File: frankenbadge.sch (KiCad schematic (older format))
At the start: 42 parts, among them IC101 PIC32MX270, P101 CONN_01X05, P102 USB_A, Q101 Q_NPN_BEC, Q102 Q_NPN_BEC, SW101 SW_PUSH, U101 4MHz resonator, U102 MCP1623/24, U103 MCP1700T, U104 TSOP362, U105 TouchSensor, U106 TouchSensor, Y101 32.768kHz

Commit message: cleaned up some caps and jumpers
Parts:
- removed C111: 0.1u, symbol C_Small
- added R101, R102, R113: 0R0, symbol R_Small
- added R107: 1K0, symbol R_Small
- C110: value 1u -> 0.1u
- renumbered R101 to R103, R102 to R104, R103 to R105, R104 to R106, R105 to R108, R106 to R109, R107 to R110, R108 to R111, R109 to R112, R110 to R114, R111 to R115, R112 to R116, R113 to R117
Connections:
- wire segments 164 -> 171
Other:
- moved on the sheet: C110

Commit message: updated boost converter parts and added screen interface
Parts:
- BT101: symbol Battery -> Battery-RESCUE-frankenbadge
- C103: value Cin -> 4.7u
- C105: value Cout -> 10u
- D101: symbol LED -> LED-RESCUE-frankenbadge
- D102: symbol LED_RGB -> LED_RGB-RESCUE-frankenbadge
- L101: value L_Small -> 4.7 uH; Fieldname (none) -> Value
- P102: symbol USB_A -> USB_A-RESCUE-frankenbadge
- R103: value Rt -> 3011
- R104: value Rb -> 6041
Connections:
- net labels added: /CS, /RES, AO, LEDK, SCA, SCK
- wire segments 171 -> 178
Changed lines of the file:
@@
 $Descr A4 11693 8268
 encoding utf-8
-Sheet 1 1
+Sheet 1 2
 Title ""
 Date ""
@@
 $EndComp
 $Comp
-L Battery BT101
+L Battery-RESCUE-frankenbadge BT101
 U 1 1 58485CE3
 P 720 940
@@
 P 960 930
 F 0 "C103" H 970 1000 50  0000 L CNN
-F 1 "Cin" H 970 850 50  0000 L CNN
+F 1 "4.7u" H 970 850 50  0000 L CNN
 F 2 "" H 960 930 50  0000 C CNN
 F 3 "" H 960 930 50  0000 C CNN
@@
 P 1170 690
 F 0 "L101" V 1120 650 50  0000 L CNN
-F 1 "L_Small" V 1240 540 50  0000 L CNN
+F 1 "4.7 uH" V 1240 540 50  0000 L CNN
 F 2 "" H 1170 690 50  0000 C CNN
 F 3 "" H 1170 690 50  0000 C CNN
+F 4 "Value" H 1170 690 60  0001 C CNN "Fieldname"
 	1    1170 690
 	0    -1   -1   0
@@
 P 2230 910
 F 0 "R103" H 2260 930 50  0000 L CNN
-F 1 "Rt" H 2260 870 50  0000 L CNN
+F 1 "3011" H 2260 870 50  0000 L CNN
 F 2 "" H 2230 910 50  0000 C CNN
 F 3 "" H 2230 910 50  0000 C CNN
@@
 P 2230 1170
 F 0 "R104" H 2260 1190 50  0000 L CNN
-F 1 "Rb" H 2260 1130 50  0000 L CNN
+F 1 "6041" H 2260 1130 50  0000 L CNN
 F 2 "" H 2230 1170 50  0000 C CNN
 F 3 "" H 2230 1170 50  0000 C CNN
@@
 P 2460 1010
 F 0 "C105" H 2470 1080 50  0000 L CNN
-F 1 "Cout" H 2230 1010 50  0000 L CNN
+F 1 "10u" H 2230 1010 50  0000 L CNN
 F 2 "" H 2460 1010 50  0000 C CNN
 F 3 "" H 2460 1010 50  0000 C CNN
@@
 $EndComp
 $Comp
-L USB_A P102
+L USB_A-RESCUE-frankenbadge P102
 U 1 1 5848AEBB
 P 8520 2570
@@
 	1960 3860 1750 3860
 Wire Wire Line
-	1750 3860 1750 3820
-Wire Wire Line
-	1750 3820 870  3820
+	1750 3820 1750 3860
+Wire Wire Line
+	870  3820 1750 3820
 Wire Wire Line
 	1960 3980 1750 3980
 Wire Wire Line
-	1750 3980 1750 4020
-Wire Wire Line
-	1750 4020 870  4020
+	1750 4020 1750 3980
+Wire Wire Line
+	870  4020 1750 4020
 Connection ~ 1510 4020
 Connection ~ 1510 3820
@@
 Connection ~ 2640 6180
 $Comp
-L LED_RGB D102
+L LED_RGB-RESCUE-frankenbadge D102
 U 1 1 5848EC5B
 P 5630 3310
@@
 	4460 6300 4460 6300
 $Comp
-L LED D101
+L LED-RESCUE-frankenbadge D101
 U 1 1 58491021
 P 4770 5900
@@
 $EndComp
 Wire Wire Line
-	5690 2570 4720 2570
-Wire Wire Line
-	4720 2570 4720 3770
-Wire Wire Line
-	4720 3770 3960 3770
+	5690 2570 4800 2570
+Wire Wire Line
+	4800 2570 4800 3770
+Wire Wire Line
+	4800 3770 3960 3770
 $Comp
 L +3.3V #PWR122
@@
 $EndComp
 Wire Wire Line
-	3960 3870 4360 3870
-Wire Wire Line
-	4360 3870 4360 1860
-Wire Wire Line
-	4360 1860 6770 1860
-Wire Wire Line
-	4500 2040 6770 2040
-Wire Wire Line
-	4500 2040 4500 3970
-Wire Wire Line
-	4500 3970 3960 3970
+	3960 3870 4695 3870
+Wire Wire Line
+	4695 3870 4695 1860
+Wire Wire Line
+	4695 1860 6770 1860
+Wire Wire Line
+	4765 2045 6770 2040
+Wire Wire Line
+	4765 2045 4765 3975
+Wire Wire Line
+	4765 3975 3960 3970
 $Comp
 L GND #PWR128
@@
 	7370 1370 7370 2240
 Wire Wire Line
-	3960 3570 4070 3570
-Wire Wire Line
-	4070 3570 4070 1280
-Wire Wire Line
-	4070 1280 6770 1280
-Wire Wire Line
-	6770 1460 4180 1460
-Wire Wire Line
-	4180 1460 4180 3670
-Wire Wire Line
-	4180 3670 3960 3670
+	3960 3570 4465 3570
+Wire Wire Line
+	4465 3570 4465 1280
+Wire Wire Line
+	4465 1280 6770 1280
+Wire Wire Line
+	6770 1460 4610 1460
+Wire Wire Line
+	4610 1460 4610 3670
+Wire Wire Line
+	4610 3670 3960 3670
 Connection ~ 7370 1950
 $Comp
@@
 Wire Wire Line
 	5150 2380 5040 2380
+$Sheet
+S 8675 4100 1505 1235
+U 591A14A3
+F0 "screen" 60
+F1 "screen.sch" 60
+F2 "/CS" I L 8675 5045 60
+F3 "SCK" I L 8675 4325 60
+F4 "SDA" I L 8675 4520 60
+F5 "AO" I L 8675 4690 60
+F6 "/RESET" I L 8675 4865 60
+F7 "PWR" I L 8675 4175 60
+F8 "LEDK" I L 8675 5230 60
+$EndSheet
+$Comp
+L +3.3V #PWR?
+U 1 1 591A3ACB
+P 8365 4175
+F 0 "#PWR?" H 8365 4025 50  0001 C CNN
+F 1 "+3.3V" H 8365 4315 50  0000 C CNN
+F 2 "" H 8365 4175 50  0000 C CNN
+F 3 "" H 8365 4175 50  0000 C CNN
+F 4 "Value" H 8365 4175 60  0001 C CNN "Fieldname"
+	1    8365 4175
+	1    0    0    -1
+$EndComp
+Wire Wire Line
+	8675 4175 8365 4175
+Wire Wire Line
+	8675 4325 8120 4325
+Wire Wire Line
+	8675 4520 8120 4520
+Wire Wire Line
+	8675 4690 8120 4690
+Wire Wire Line
+	8675 4865 8120 4865
+Wire Wire Line
+	8675 5045 8120 5045
+Wire Wire Line
+	8675 5230 8120 5230
+Text Label 8120 4325 0    60   ~ 0
+SCK
+Text Label 8120 4520 0    60   ~ 0
+SCA
+Text Label 8120 4690 0    60   ~ 0
+AO
+Text Label 8120 4865 0    60   ~ 0
+/RES
+Text Label 8120 5045 0    60   ~ 0
+/CS
+Text Label 8120 5230 0    60   ~ 0
+LEDK
+Text Label 3960 2370 0    60   ~ 0
+SCK
 $EndSCHEMATC

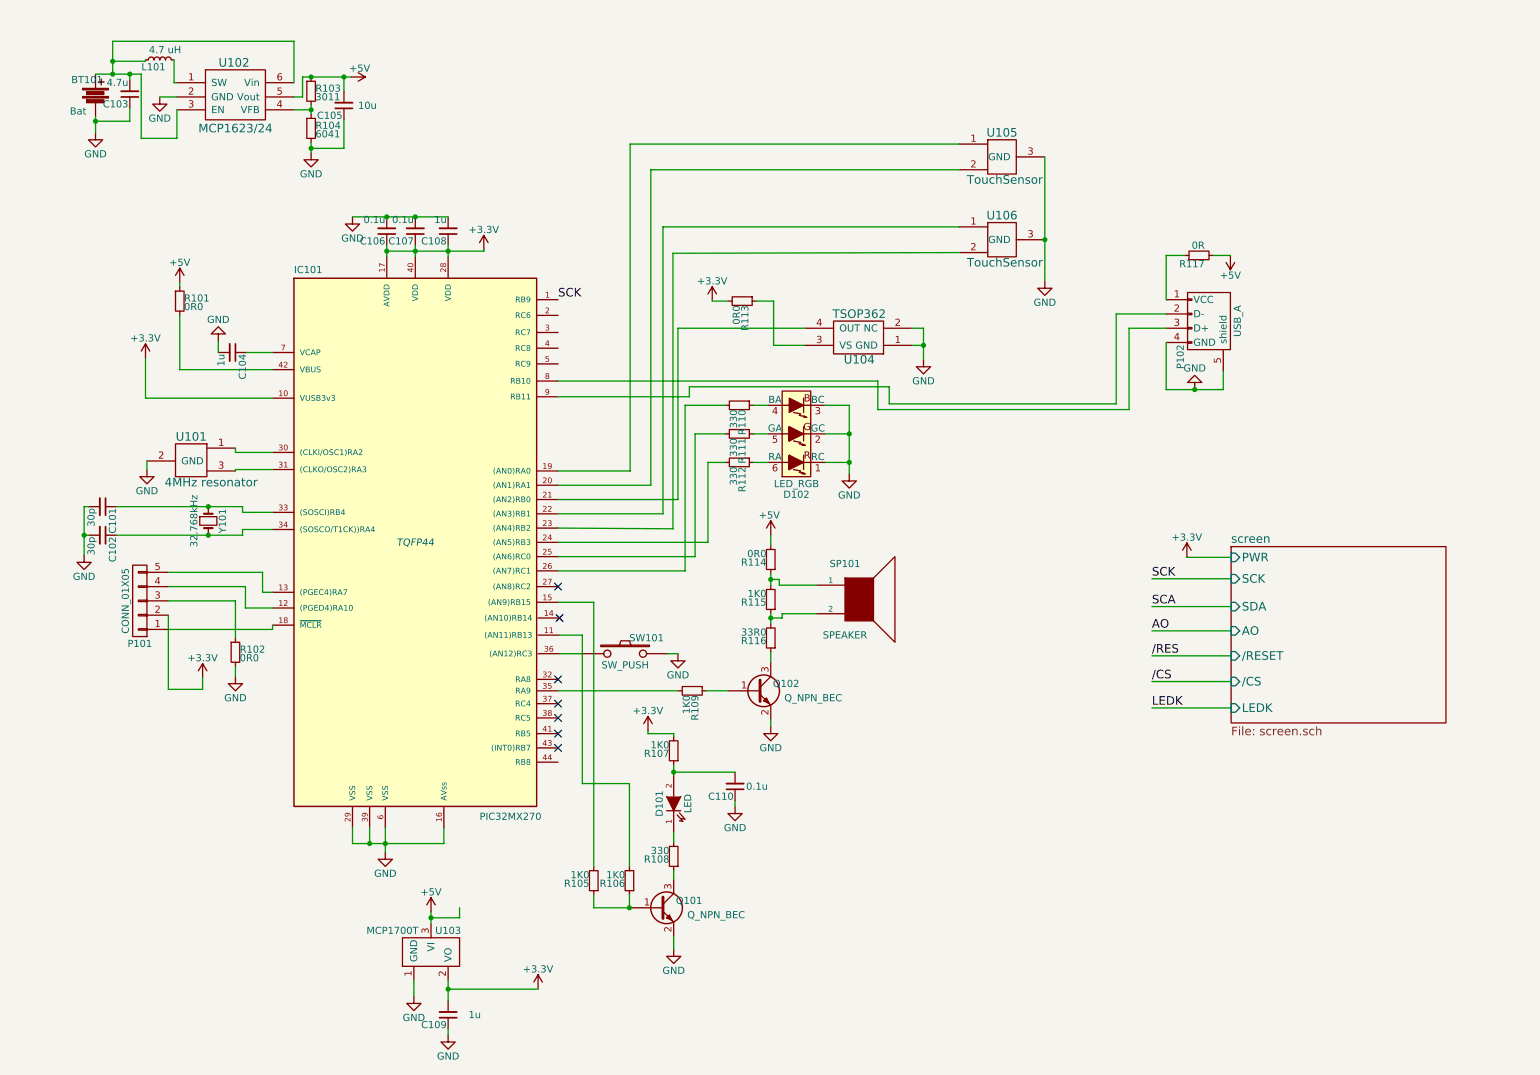
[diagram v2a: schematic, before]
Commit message: moved power circuits to separate sheet and used Vusb label for input to buck converter
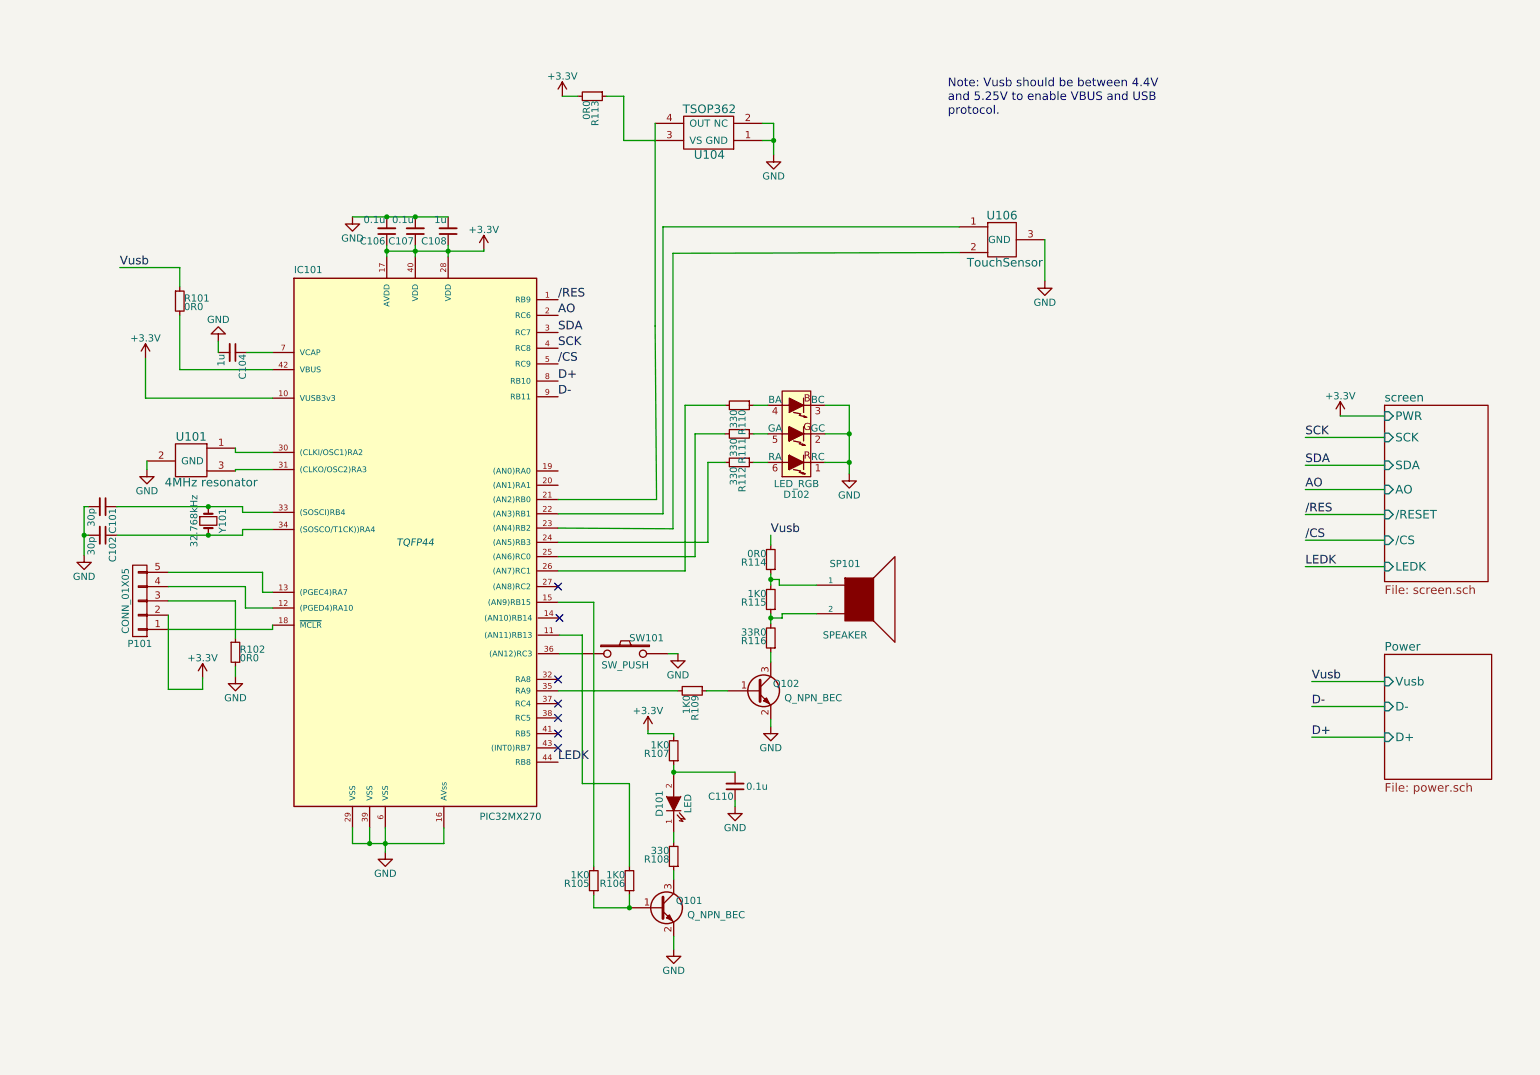
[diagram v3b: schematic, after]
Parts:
- removed BT101: Bat, symbol Battery-RESCUE-frankenbadge
- removed C103: 4.7u, symbol C_Small
- removed C105: 10u, symbol C_Small
- removed C109: 1u, symbol C_Small
- removed L101: 4.7 uH, symbol L_Small
- removed P102: USB_A, symbol USB_A-RESCUE-frankenbadge
- removed R103: 3011, symbol R_Small
- removed R104: 6041, symbol R_Small
- removed R117: 0R, symbol R_Small
- removed U102: MCP1623/24, symbol MCP1623/24
- removed U103: MCP1700T, symbol MCP1700T
- removed U105: TouchSensor, symbol TouchSensor
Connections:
- net /CS: now also IC101.5 (RC9)
- net /RES: now also IC101.1 (RB9)
- net AO: now also IC101.2 (RC6)
- net LEDK: now also IC101.44 (RB8)
- net SCK: now also IC101.4 (RC8); no longer IC101.1 (RB9)
- net SDA: now reaches IC101.3 (RC7)
- net D+: now reaches IC101.8 (RB10)
- net D-: now reaches IC101.9 (RB11)
- net +5V renamed Vusb
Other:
- note added: "Note: Vusb should be between 4.4V \nand 5.25V to enable VBUS and USB \nprotocol."
- moved on the sheet: R113, U104

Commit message: cleaned up schematic, updated ir receive/transmit
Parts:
- removed R105, R106, R107: 1K0, symbol R_Small
- removed R113: 0R0, symbol R_Small
- removed U104: TSOP362, symbol TSOP362
- added R102: 4.7K, symbol R_Small
- added SW102, SW103, SW104, SW105: SW_PUSH, symbol SW_PUSH
- added U?: TSOP39338, symbol TSOP39338
- D101: value LED -> TSKS5400S; Fieldname (none) -> Value
- renumbered C104 to C103, C106 to C104, C107 to C105, C108 to C106, C110 to C107, R102 to R103, R108 to R104, R109 to R105, R110 to R106, R111 to R107, R112 to R108, R114 to R109, R115 to R110, R116 to R111, U106 to U103
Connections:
- net +3V3: now also C107.2, D101.2 (A), R102.1, U?.2 (VS)
- net GND: now also SW102.2, SW103.2, SW104.2, SW105.2, U?.3 (GND)
- net at IC101.18 (~MCLR), P101.1 (P1): now also R102.2
- net at IC101.11 ((AN11)RB13): now also Q101.1 (B)
- net SW_U: now reaches IC101.14 ((AN10)RB14)
- net SW_U: now also SW103.1
- net SW_L: now reaches IC101.15 ((AN9)RB15)
- net SW_L: now also SW102.1
- net SW_R: now reaches IC101.19 ((AN0)RA0)
- net SW_R: now also SW105.1
- net SW_D: now reaches IC101.20 ((AN1)RA1)
- net SW_D: now also SW104.1
- net at IC101.21 ((AN2)RB0): now also U?.1 (OUT)
- net at IC101.24 ((AN5)RB3): now also R106.2; no longer R108.2
- net at IC101.26 ((AN7)RC1): now also R108.2; no longer R106.2
- net at D102.4 (BA): now also R108.1; no longer R106.1
- net at D102.6 (RA): now also R106.1; no longer R108.1
- no-connect marks 7 -> 6
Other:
- moved on the sheet: C107, D101, Q101, Q102, R104, R109, R110, R111, SP101
